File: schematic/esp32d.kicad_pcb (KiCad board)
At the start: 2 copper layers, 86.4 x 51.4 mm, 47 parts, among them IC1 CP2102N-A01-GQFN28R, J1 Conn_02x08_Odd_Even, J2 Conn_02x08_Odd_Even, J4 Conn_01x02, Q1 SS8050-G, Q2 SS8050-G, Q3 DMG2307L-7, SW1 SW_Push, U1 AMS1117-3.3, U2 ESP32-WROOM-32D, U3 DizzyBITLogo, U4 MCP73831-2-OT, U5 DizzyBIT-Layout

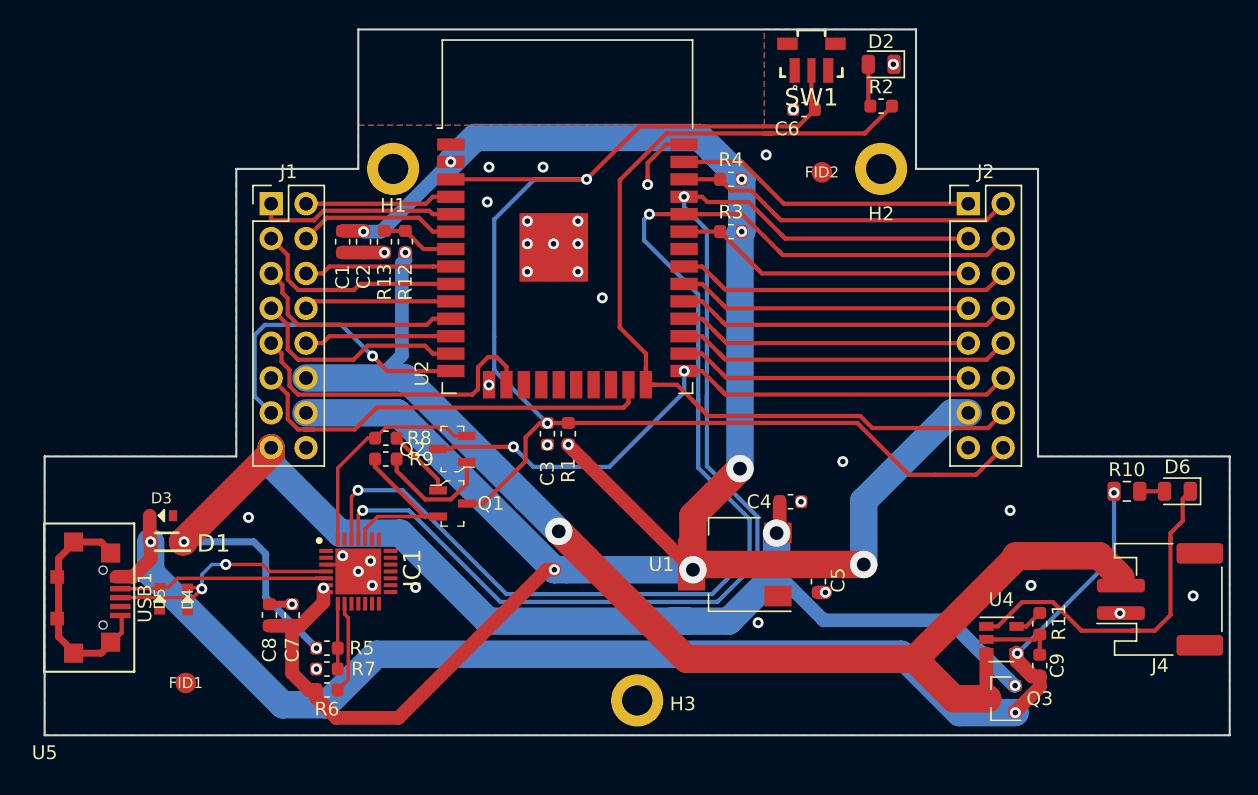
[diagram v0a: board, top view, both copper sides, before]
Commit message: Major Update. Changed pin configuration and board outline.
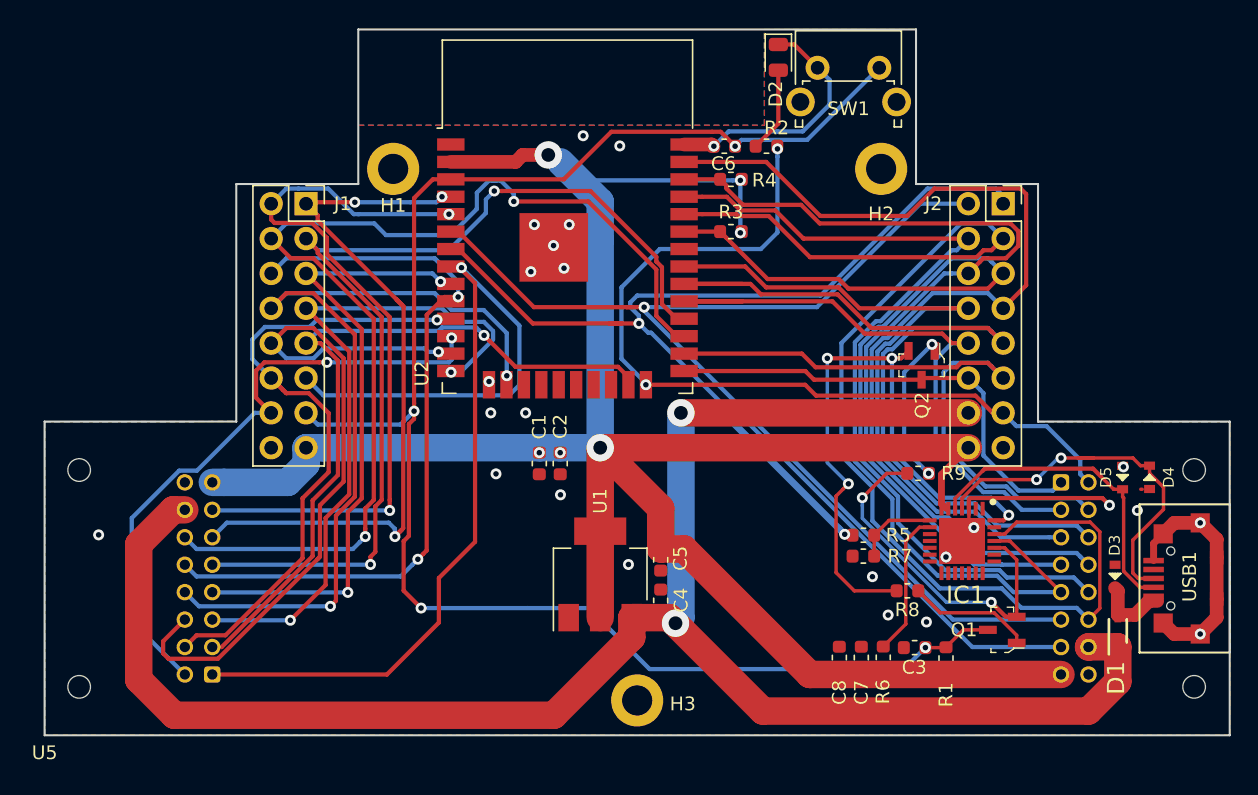
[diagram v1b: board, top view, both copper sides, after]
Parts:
- removed C9: C4.7uF/6.3V(20%), Capacitor_SMD:C_0603_1608Metric
- removed D6: LED-YELLOW, LED_SMD:LED_0805_2012Metric
- removed FID1, FID2: FIDUCIAL-1.5mm, fab:FIDUCIAL-1.5mm
- removed Q3: DMG2307L-7, Package_TO_SOT_SMD:SOT-23
- removed R10: R1K, Resistor_SMD:R_0805_2012Metric
- removed R11: R4.7K, Resistor_SMD:R_0603_1608Metric
- removed R12, R13: R100K, Resistor_SMD:R_0603_1608Metric
- removed U4: MCP73831-2-OT, Package_TO_SOT_SMD:SOT-23-5
- added J3: Conn_02x08_Odd_Even, Connector_JST:JST_PUD_S16B-PUDSS-1_2x08_P2.00mm_Horizontal, B.Cu at (150.3, 127.6)
- J1, J2: footprint Connector_PinHeader_2.54mm:PinHeader_2x08_P2.54mm_Vertical -> Connector_PinSocket_2.54mm:PinSocket_2x08_P2.54mm_Vertical
- J4: value Conn_01x02 -> Conn_02x08_Odd_Even; footprint Connector_JST:JST_PH_S2B-PH-SM4-TB_1x02-1MP_P2.00mm_Horizontal -> Connector_JST:JST_PUD_S16B-PUDSS-1_2x08_P2.00mm_Horizontal; moved to B.Cu
- SW1: footprint Button_Switch_SMD:TL3340 -> Button_Switch_THT:SW_Tactile_SPST_Angled_PTS645Vx31-2LFS
- moved D5 70.7 mm to (154.8, 127.3), turned to 90 degrees
- moved USB1 70.7 mm to (154.7, 134.6), turned to 90 degrees
- moved D4 70.7 mm to (156.7, 127.3)
- moved D3 69.6 mm to (154.2, 134.5), turned to 90 degrees
- moved D1 69.6 mm to (154.4, 138.4), turned to 90 degrees
- moved J4 69.3 mm to (88.4, 141.6)
- moved IC1 44.0 mm to (143.1, 131.9), turned to 270 degrees
- moved C8 41.6 mm to (134.1, 140.4)
- moved C7 41.6 mm to (135.7, 140.4)
- moved Q1 41.1 mm to (146.0, 138.4), turned to 180 degrees
- moved R6 40.6 mm to (137.3, 140.4), turned to 270 degrees
- moved R5 39.9 mm to (135.9, 131.5)
- moved R7 39.9 mm to (135.9, 133.0)
- moved R8 39.6 mm to (139.1, 135.5)
- moved R9 38.8 mm to (139.9, 127.0)
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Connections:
- J1 pad 1: I39 -> I36
- J1 pad 10: IO27 -> HSPI_CLK
- J1 pad 11: IO15 -> IO32
- J1 pad 12: VBAT -> IO26
- J1 pad 13: HSPI_MISO -> EN
- J1 pad 14: +3.3V -> IO27
- J1 pad 15: EXT_5V -> +3.3V
- J1 pad 2: I36 -> I39
- J1 pad 3: IO33 -> IO17
- J1 pad 4: I34 -> IO16
- J1 pad 5: IO26 -> IO33
- J1 pad 6: IO32 -> IO25
- J1 pad 7: HSPI_CLK -> HSPI_MISO
- J1 pad 8: IO25 -> HSPI_MOSI
- J1 pad 9: HSPI_MOSI -> IO15
- J2 pad 1: VSPI_MOSI -> I35
- J2 pad 10: IO16 -> IO5
- J2 pad 13: +3.3V -> IO2
- J2 pad 14: IO2 -> EXT_5V
- J2 pad 16: EN -> +3.3V
- J2 pad 2: I2C_SCL -> I34
- J2 pad 3: IO1 -> IO3
- J2 pad 4: IO3 -> IO1
- J2 pad 6: VSPI_MISO -> I2C_SCL
- J2 pad 7: VSPI_CLK -> VSPI_MOSI
- J2 pad 8: IO5 -> VSPI_MISO
- J2 pad 9: IO17 -> VSPI_CLK
- J4 pad 1: GND -> IO32
- J4 pad 2: VBAT -> IO27
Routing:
- net VBAT: track 115.0 -> 0.00 mm, vias 2 -> 0
- net VBUS: track 102.7 -> 5.34 mm, vias 4 -> 0
- net I35: track 5.38 -> 90.8 mm, vias 0 -> 1
- net I34: track 11.6 -> 83.6 mm, vias 0 -> 1
- net IO32: track 10.8 -> 72.9 mm, vias 0 -> 1
- net IO16: track 24.9 -> 80.4 mm, vias 0 -> 2
- net VSPI_MOSI: track 22.0 -> 75.1 mm
- net IO17: track 22.5 -> 73.8 mm, vias 0 -> 2
- net EXT_5V: track 101.7 -> 151.5 mm, vias 4 -> 3
- net I2C_SDA: track 23.1 -> 69.0 mm
- net IO25: track 10.8 -> 55.6 mm, vias 0 -> 2
- net I36: track 10.8 -> 54.1 mm, vias 0 -> 3
- net VSPI_CLK: track 21.7 -> 63.9 mm
- net I2C_SCL: track 25.4 -> 66.7 mm
- net I39: track 14.7 -> 54.7 mm, vias 0 -> 2
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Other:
- outline, holes or cut-outs redrawn
- board text added: "DizzyBit - ESP32D - V 1.0.4"
